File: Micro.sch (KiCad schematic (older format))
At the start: 22 parts, among them J2 Conn_01x02_Male, J3 Conn_01x08_Male, J4 Conn_01x02_Male, J5 Conn_ARM_JTAG_SWD_10, U7 CC7V_T1A_32.768KHZ, U8 BT832L, U9 MIC9409

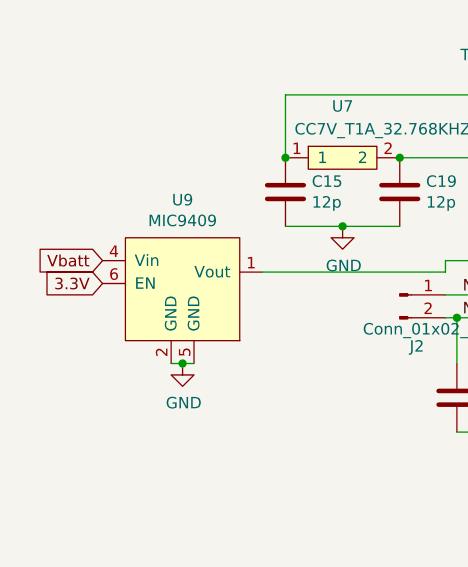
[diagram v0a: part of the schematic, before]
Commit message: Connected high side power switcher enable pin to SHDN net instead of 3.3V. Prevents feedback on the 3.3V net from registering as a logic high and keeping the power going through
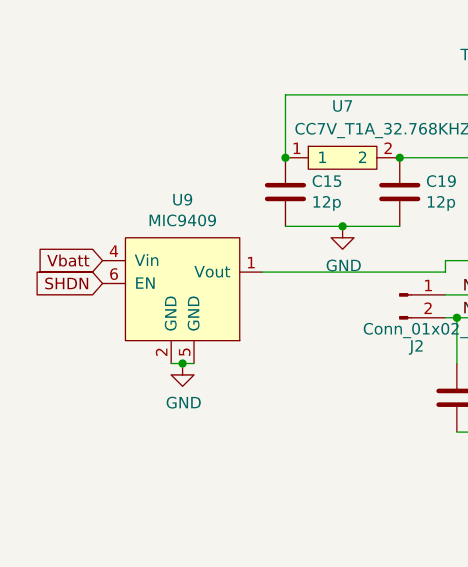
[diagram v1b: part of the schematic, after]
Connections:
- net 3.3V: no longer U9.6 (EN)
- new net SHDN: U9.6 (EN)
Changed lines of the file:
@@
 	1    0    0    -1
 $EndComp
-Text GLabel 2275 3775 0    50   Input ~ 0
-3.3V
 Wire Wire Line
 	3075 3525 3325 3525
@@
 Text GLabel 7075 3275 2    50   Input ~ 0
 LEAD_DETECT
+Text GLabel 2275 3775 0    50   Input ~ 0
+SHDN
 $EndSCHEMATC

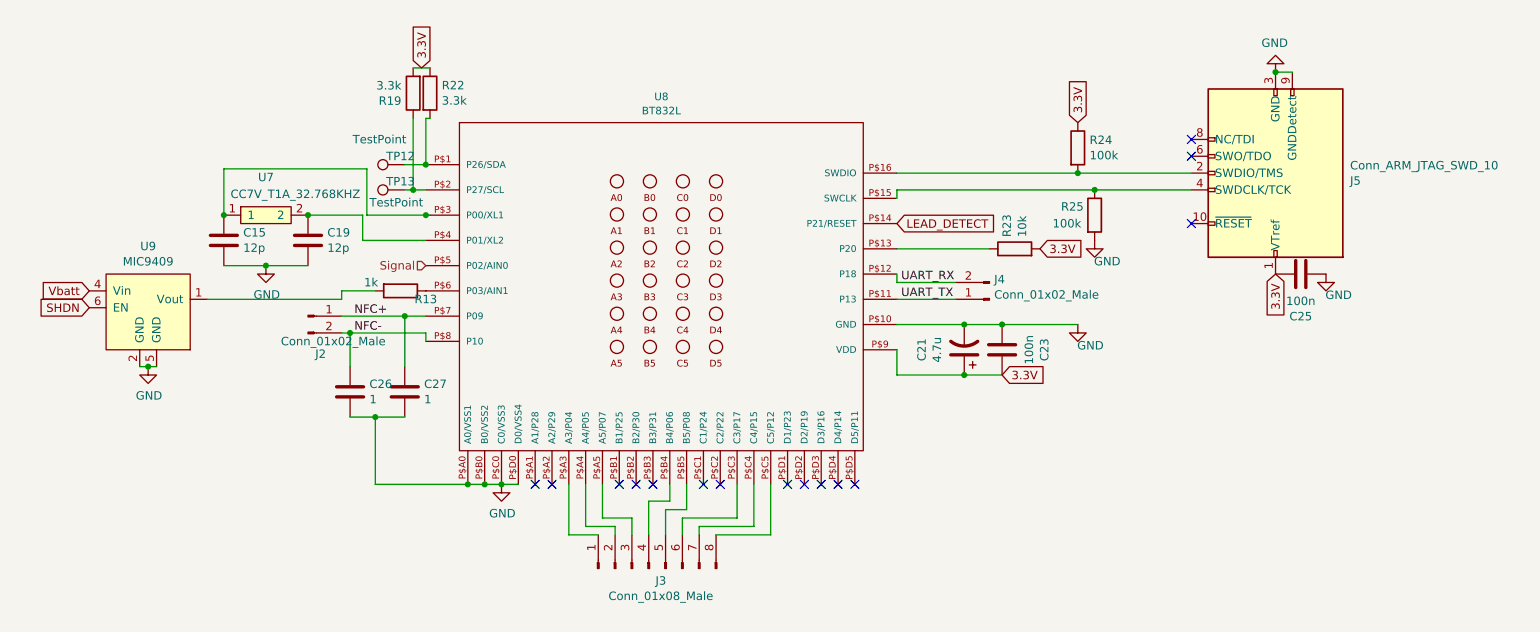
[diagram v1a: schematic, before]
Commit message: #25 - Updated low pass filter. Gain 2x -> 1x. Added ADC divider for battery to account for brand new batteries.
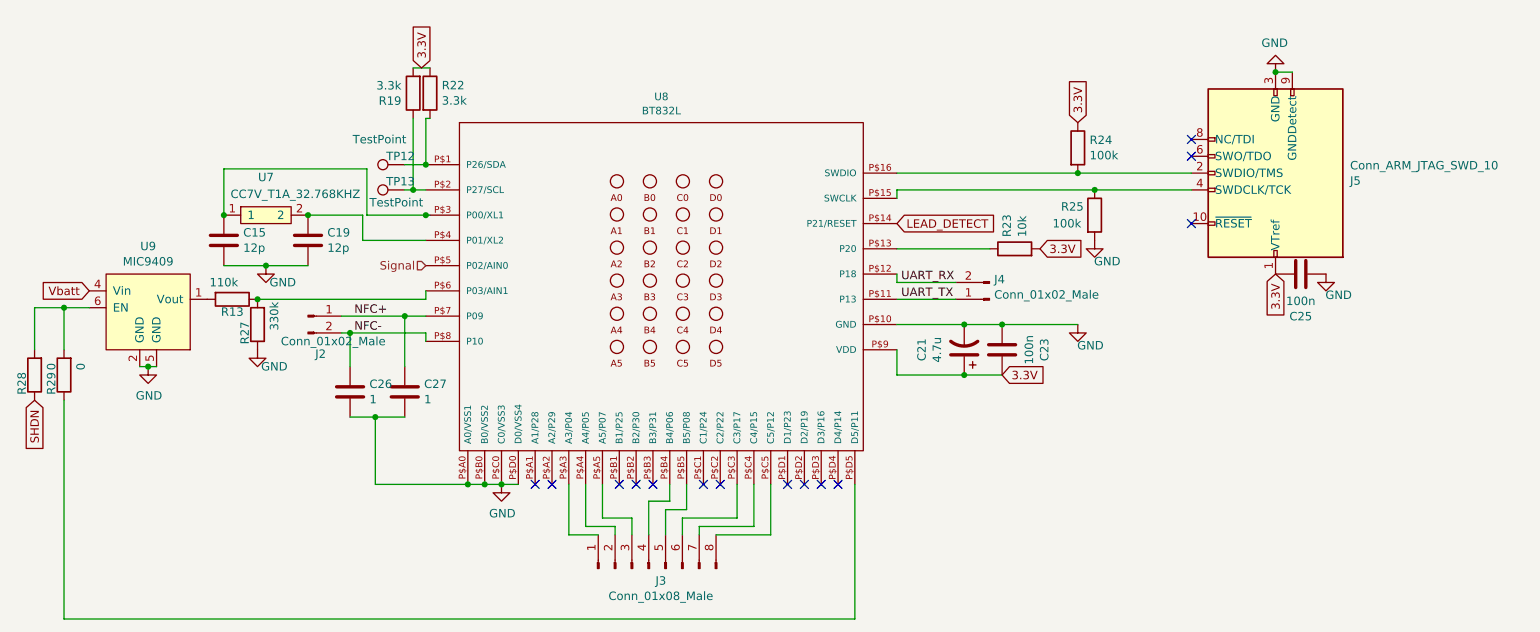
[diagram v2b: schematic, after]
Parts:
- added R27: 330k, Resistor_SMD:R_0805_2012Metric_Pad1.20x1.40mm_HandSolder, symbol Device:R
- added R28, R29: 0, Resistor_SMD:R_0402_1005Metric_Pad0.72x0.64mm_HandSolder, symbol Device:R
- R13: value 1k -> 110k
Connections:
- net GND: now also R27.1
- net SHDN: now also R28.1; no longer U9.6 (EN)
- net at R13.1, U8.P$6 (P03/AIN1): now also R27.2
- net at U8.P$D5 (D5/P11): now also R29.1
- new net: R28.2, R29.2, U9.6 (EN)
- no-connect marks 15 -> 14
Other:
- moved on the sheet: R13
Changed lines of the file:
@@
 NoConn ~ 6625 4825
 NoConn ~ 6725 4825
-NoConn ~ 6825 4825
 $Comp
 L Connector:Conn_01x02_Male J2
@@
 L Device:R R13
 U 1 1 5FE7D3BE
-P 4125 3675
-F 0 "R13" V 4175 3825 50  0000 C CNN
-F 1 "1k" V 4075 3500 50  0000 C CNN
-F 2 "Resistor_SMD:R_0805_2012Metric_Pad1.20x1.40mm_HandSolder" V 4055 3675 50  0001 C CNN
-F 3 "~" H 4125 3675 50  0001 C CNN
-	1    4125 3675
+P 3125 3725
+F 0 "R13" V 3200 3725 50  0000 C CNN
+F 1 "110k" V 3025 3675 50  0000 C CNN
+F 2 "Resistor_SMD:R_0805_2012Metric_Pad1.20x1.40mm_HandSolder" V 3055 3725 50  0001 C CNN
+F 3 "~" H 3125 3725 50  0001 C CNN
+	1    3125 3725
 	0    1    1    0
 $EndComp
-Wire Wire Line
-	3975 3675 3775 3675
 $Comp
 L Oscillators:CC7V_T1A_32.768KHZ U7
@@
 P 3325 3525
 F 0 "#PWR015" H 3325 3275 50  0001 C CNN
-F 1 "GND" H 3330 3352 50  0000 C CNN
+F 1 "GND" H 3425 3425 50  0000 C CNN
 F 2 "" H 3325 3525 50  0001 C CNN
 F 3 "" H 3325 3525 50  0001 C CNN
@@
 Connection ~ 7700 3875
 NoConn ~ 8825 3275
-Wire Wire Line
-	3775 3725 3775 3675
 Connection ~ 3075 3225
 Connection ~ 3325 3525
@@
 Text GLabel 2275 3675 0    50   Input ~ 0
 Vbatt
-Wire Wire Line
-	3775 3725 2975 3725
 Text GLabel 7075 3275 2    50   Input ~ 0
 LEAD_DETECT
-Text GLabel 2275 3775 0    50   Input ~ 0
+Text GLabel 1950 4325 3    50   Input ~ 0
 SHDN
+$Comp
+L Device:R R27
+U 1 1 60632C79
+P 3275 3875
+F 0 "R27" V 3350 3925 50  0000 C CNN
+F 1 "330k" V 3175 3825 50  0000 C CNN
+F 2 "Resistor_SMD:R_0805_2012Metric_Pad1.20x1.40mm_HandSolder" V 3205 3875 50  0001 C CNN
+F 3 "~" H 3275 3875 50  0001 C CNN
+	1    3275 3875
+	-1   0    0    1
+$EndComp
+$Comp
+L power:GND #PWR024
+U 1 1 606330F2
+P 3275 4025
+F 0 "#PWR024" H 3275 3775 50  0001 C CNN
+F 1 "GND" H 3375 3925 50  0000 C CNN
+F 2 "" H 3275 4025 50  0001 C CNN
+F 3 "" H 3275 4025 50  0001 C CNN
+	1    3275 4025
+	1    0    0    -1
+$EndComp
+Wire Wire Line
+	3275 3725 4275 3725
+Wire Wire Line
+	4275 3725 4275 3675
+Connection ~ 3275 3725
+$Comp
+L Device:R R28
+U 1 1 60649913
+P 1950 4175
+F 0 "R28" V 2025 4225 50  0000 C CNN
+F 1 "0" V 1850 4125 50  0000 C CNN
+F 2 "Resistor_SMD:R_0402_1005Metric_Pad0.72x0.64mm_HandSolder" V 1880 4175 50  0001 C CNN
+F 3 "~" H 1950 4175 50  0001 C CNN
+	1    1950 4175
+	-1   0    0    1
+$EndComp
+$Comp
+L Device:R R29
+U 1 1 6064A1CA
+P 2125 4175
+F 0 "R29" V 2200 4225 50  0000 C CNN
+F 1 "0" V 2025 4125 50  0000 C CNN
+F 2 "Resistor_SMD:R_0402_1005Metric_Pad0.72x0.64mm_HandSolder" V 2055 4175 50  0001 C CNN
+F 3 "~" H 2125 4175 50  0001 C CNN
+	1    2125 4175
+	-1   0    0    1
+$EndComp
+Wire Wire Line
+	1950 4025 1950 3775
+Wire Wire Line
+	2125 4025 2125 3775
+Wire Wire Line
+	1950 3775 2125 3775
+Connection ~ 2125 3775
+Wire Wire Line
+	2125 3775 2275 3775
+Wire Wire Line
+	2125 4325 2125 5625
+Wire Wire Line
+	2125 5625 6825 5625
+Wire Wire Line
+	6825 5625 6825 4825
 $EndSCHEMATC

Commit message: #28 - Remove pulldown from reset line on micro
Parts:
- removed R23: 10k, Resistor_SMD:R_0805_2012Metric_Pad1.20x1.40mm_HandSolder, symbol Device:R
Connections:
- net LEAD_DETECT: now also U8.P$13 (P20); no longer U8.P$14 (P21/RESET)
- no-connect marks 14 -> 15
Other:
- note added: "Internally pulled up."
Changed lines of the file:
@@
 Text Label 7100 3625 0    50   ~ 0
 UART_RX
-$Comp
-L Device:R R23
-U 1 1 5FF2C8D1
-P 7775 3425
-F 0 "R23" H 7845 3471 50  0000 L CNN
-F 1 "10k" H 7845 3380 50  0000 L CNN
-F 2 "Resistor_SMD:R_0805_2012Metric_Pad1.20x1.40mm_HandSolder" V 7705 3425 50  0001 C CNN
-F 3 "~" H 7775 3425 50  0001 C CNN
-	1    7775 3425
-	0    -1   -1   0
-$EndComp
-Wire Wire Line
-	7625 3425 7075 3425
-Text GLabel 7925 3425 2    50   Input ~ 0
-3.3V
 NoConn ~ 8825 2875
 Connection ~ 9325 2375
@@
 Text GLabel 2275 3675 0    50   Input ~ 0
 Vbatt
-Text GLabel 7075 3275 2    50   Input ~ 0
-LEAD_DETECT
 Text GLabel 1950 4325 3    50   Input ~ 0
 SHDN
@@
 Wire Wire Line
 	6825 5625 6825 4825
+Text GLabel 7075 3425 2    50   Input ~ 0
+LEAD_DETECT
+NoConn ~ 7075 3275
+Text Notes 7125 3275 0    50   ~ 0
+Internally pulled up.
 $EndSCHEMATC

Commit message: Updated debug header to include 3.3V and GND
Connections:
- net 3.3V: now also J3.2 (Pin_2)
- net GND: now also J3.1 (Pin_1)
- net at U8.P$A3 (A3/P04): no longer J3.1 (Pin_1)
- net at U8.P$A4 (A4/P05): no longer J3.2 (Pin_2)
- no-connect marks 15 -> 17
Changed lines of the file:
@@
 $EndComp
-Wire Wire Line
-	5125 4825 5125 5125
-Wire Wire Line
-	5125 5125 5300 5125
-Wire Wire Line
-	5225 4825 5225 5075
-Wire Wire Line
-	5225 5075 5400 5075
 Wire Wire Line
 	5400 5075 5400 5125
@@
 Text Notes 7125 3275 0    50   ~ 0
 Internally pulled up.
+NoConn ~ 5125 4825
+$Comp
+L power:GND #PWR0102
+U 1 1 606869A5
+P 5100 5125
+F 0 "#PWR0102" H 5100 4875 50  0001 C CNN
+F 1 "GND" H 5105 4952 50  0000 C CNN
+F 2 "" H 5100 5125 50  0001 C CNN
+F 3 "" H 5100 5125 50  0001 C CNN
+	1    5100 5125
+	1    0    0    -1
+$EndComp
+Wire Wire Line
+	5300 5125 5100 5125
+Text GLabel 5400 5075 0    50   Input ~ 0
+3.3V
+NoConn ~ 5225 4825
 $EndSCHEMATC
